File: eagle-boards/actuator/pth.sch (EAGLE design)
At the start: 9 parts, among them IC1 ULN2003AN, IC2 ULN2003AN

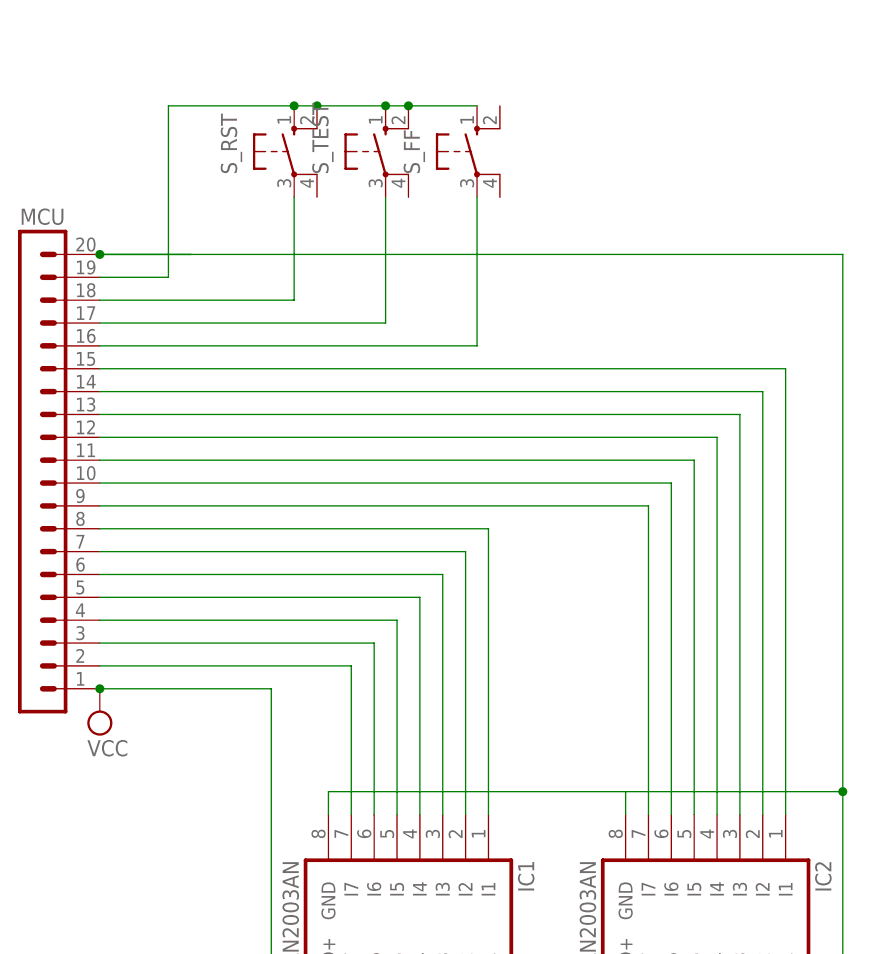
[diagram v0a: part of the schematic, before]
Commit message: New revision for the actuator board.
Fix orientation of buttons to be the same between all three, and include pull-down resistors if the input lines are not pulled down.
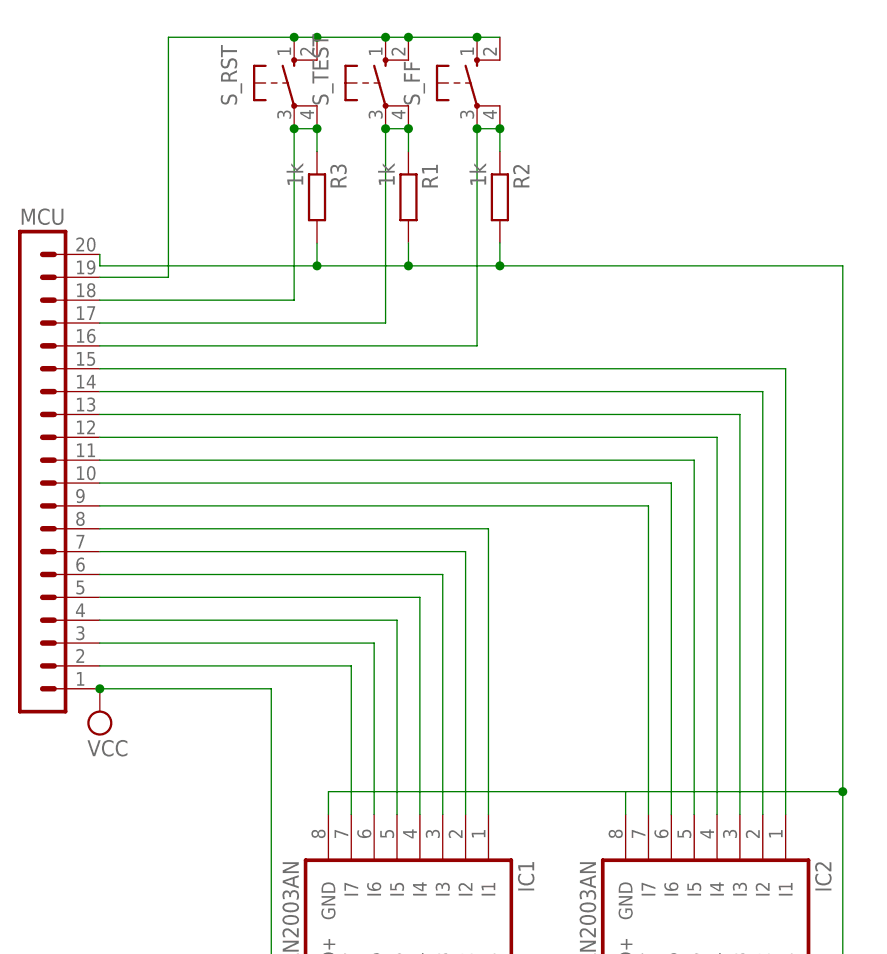
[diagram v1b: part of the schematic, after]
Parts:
- added R1, R2, R3: 1k, rcl:R-EU_0207/10
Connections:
- net GND: now also R1.2, R2.2, R3.2
- net N$17: now also R3.1, S_RST.P1
- net N$18: now also R1.1, S_TEST.P1
- net N$19: now also R2.1, S_FF.P1
- net N$2: now also S_FF.S1
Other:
- moved on the sheet: S_FF, S_RST, S_TEST
